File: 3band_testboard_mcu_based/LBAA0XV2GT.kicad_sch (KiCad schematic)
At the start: 9 parts, among them J2 Conn_Coaxial, J3 Conn_Coaxial, U4 LBAA0XV2GT-001

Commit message: Færdiggjorde GPIO
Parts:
- added C15: 100n, Capacitor_SMD:C_0603_1608Metric, symbol Device:C
- added L1: 15u, Inductor_SMD:L_Murata_DFE201610P, symbol Device:L
- added TP9: Vreg, TestPoint:TestPoint_Pad_D1.5mm, symbol Connector:TestPoint
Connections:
- net GND: now also C15.1
- net at U4.4 (VREG): now also C15.2, L1.1, TP9.1
- net at U4.6 (DCC_SW): now also L1.2
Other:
- note added: "LBAA0XV2GT-001 - 860 & 2400 MHz modem"
- note added: "TODO: debug pins ud til testpads"
- company: (none) -> AAU-connectivity
- title: (none) -> 3-band-LoRa testboard

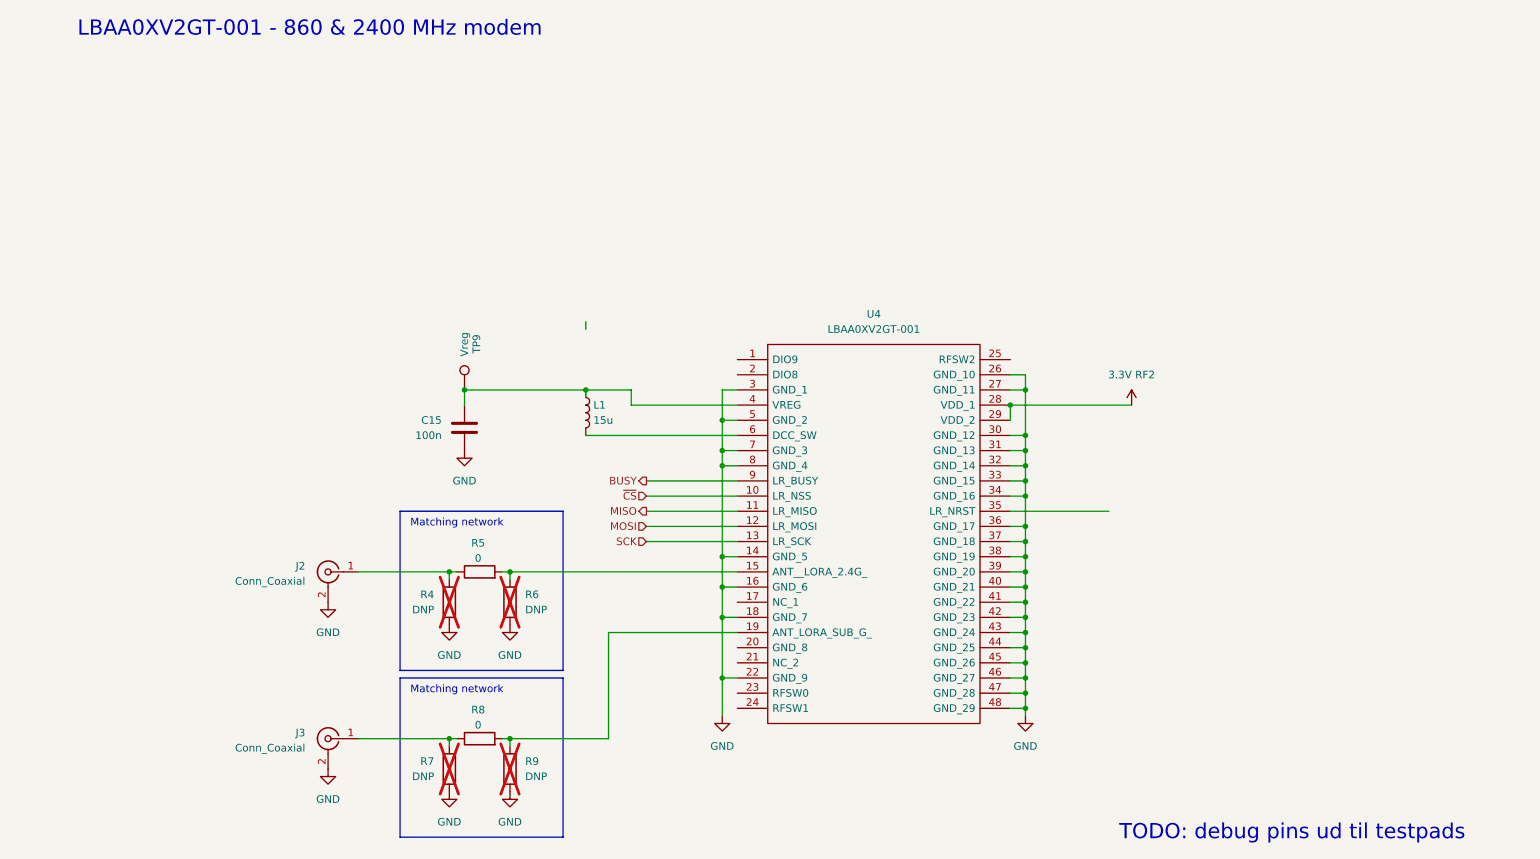
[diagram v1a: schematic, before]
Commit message: DRC check, and price
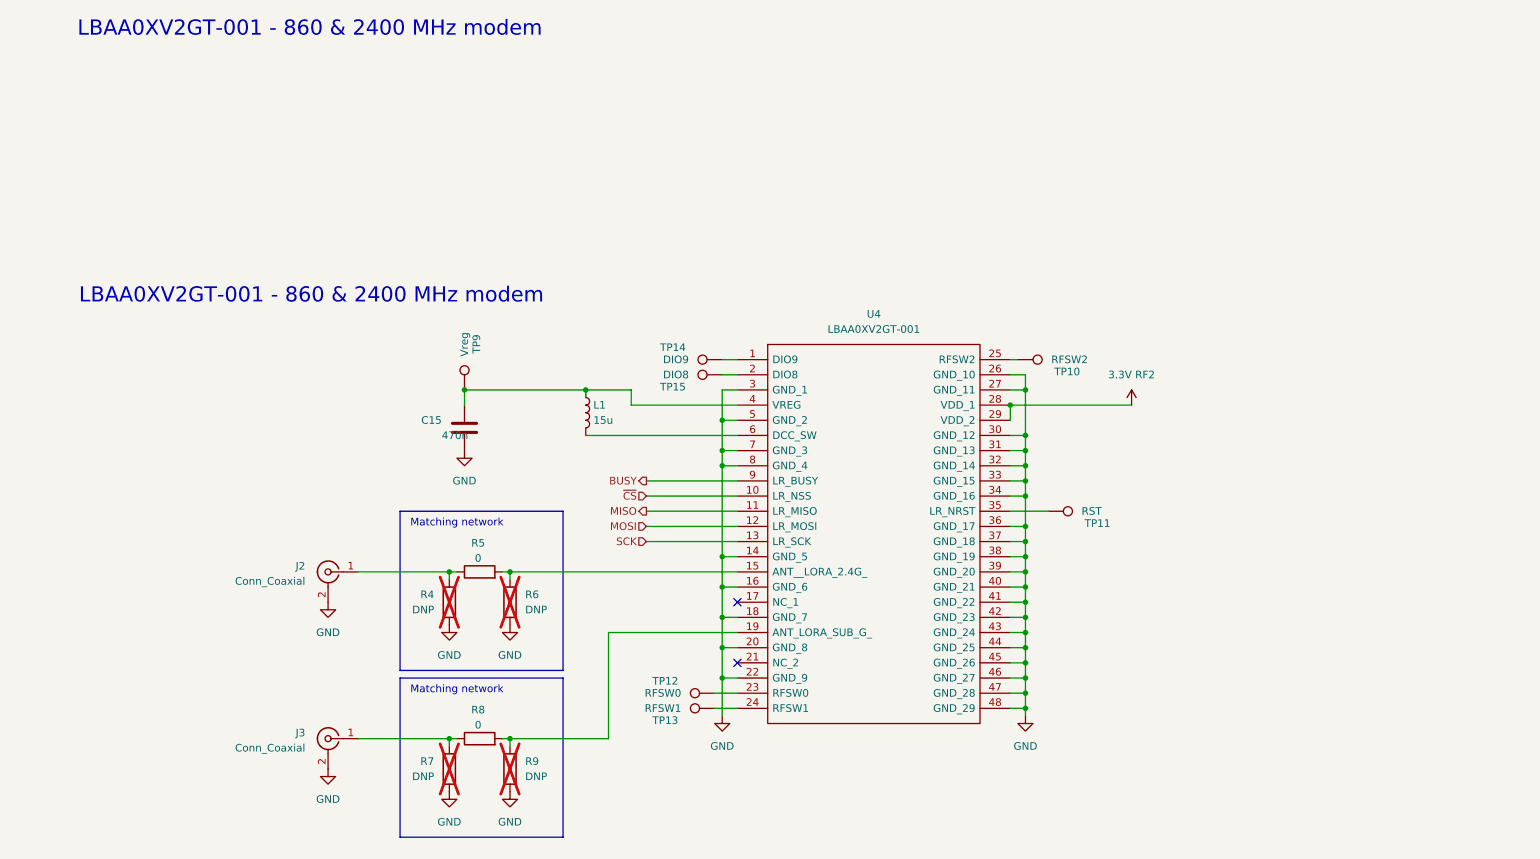
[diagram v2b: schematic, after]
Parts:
- added TP10: RFSW2, TestPoint:TestPoint_Pad_D1.5mm, symbol Connector:TestPoint
- added TP11: RST, TestPoint:TestPoint_Pad_D1.5mm, symbol Connector:TestPoint
- added TP12: RFSW0, TestPoint:TestPoint_Pad_D1.5mm, symbol Connector:TestPoint
- added TP13: RFSW1, TestPoint:TestPoint_Pad_D1.5mm, symbol Connector:TestPoint
- added TP14: DIO9, TestPoint:TestPoint_Pad_D1.5mm, symbol Connector:TestPoint
- added TP15: DIO8, TestPoint:TestPoint_Pad_D1.5mm, symbol Connector:TestPoint
- C15: value 100n -> 470n; footprint Capacitor_SMD:C_0603_1608Metric -> Capacitor_SMD:C_0805_2012Metric_Pad1.18x1.45mm_HandSolder
- J2, J3: footprint Connector_Coaxial:SMA_Amphenol_132289_EdgeMount -> Connector_Coaxial:SMA_Samtec_SMA-J-P-H-ST-EM1_EdgeMount
- L1: footprint Inductor_SMD:L_Murata_DFE201610P -> ASPI-4030S
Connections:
- net GND: now also U4.20 (GND_8)
- net at U4.1 (DIO9): now also TP14.1
- net at U4.2 (DIO8): now also TP15.1
- net at U4.23 (RFSW0): now also TP12.1
- net at U4.24 (RFSW1): now also TP13.1
- net at U4.25 (RFSW2): now also TP10.1
- net at U4.35 (LR_NRST): now also TP11.1
- no-connect marks 0 -> 2
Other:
- note removed: "TODO: debug pins ud til testpads"

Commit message: Prisoverslag
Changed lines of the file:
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@@
 	(text "LBAA0XV2GT-001 - 860 & 2400 MHz modem"
 		(exclude_from_sim no)
-		(at 60.706 61.722 0)
+		(at 59.69 17.78 0)
 		(effects
 			(font
@@
 			)
 		)
-	)
-	(text "LBAA0XV2GT-001 - 860 & 2400 MHz modem"
-		(exclude_from_sim no)
-		(at 60.452 17.018 0)
-		(effects
-			(font
-				(size 2.54 2.54)
-			)
-		)
